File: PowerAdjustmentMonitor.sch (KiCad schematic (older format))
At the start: 19 parts

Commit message: Preliminary Module Layouts
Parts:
- removed R? (x2): R, ~, symbol R
- removed U? (x2): LM324, ~, symbol LM324
- gave numbers to parts that had none: 15
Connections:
- net labels removed: V+_CURR_MON, V-_CURR_MON
- wire segments 96 -> 58

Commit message: Power Modification Module
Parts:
- removed JP2, JP3: JUMPER, ~, symbol JUMPER
- removed R20: RVAR, ~, symbol RVAR
- removed U10: LM317, ~, symbol LM317
- removed U8, U9: 7805, ~, symbol 7805
- added C14, C15, C16, C17, C18, C19, C20, C21, C22, C23, C24, C25: C, ~, symbol C
- added D10, D11, D12, D3, D6, D7, D8, D9: DIODE, ~, symbol DIODE
- added R20, R52, R53, R55: R, ~, symbol R
- added R54: RVAR, ~, symbol RVAR
- added U6: LM317, ~, symbol LM317
- added U7, U8: LM337T, TO-220, symbol LM337T
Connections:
- wire segments 58 -> 108
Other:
- note added: "-1.5 to -10V Output"
- note added: "-10V Output\n"
- note added: "1.5 to 10V Output"
- note added: "10V Output\n"
- moved on the sheet: JP1, R21, R22, R25, R26, R27, R28, U11

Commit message: November 25 Update
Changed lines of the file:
@@
 Sheet 7 9
 Title ""
-Date "27 oct 2013"
+Date "9 nov 2013"
 Rev ""
 Comp ""
@@
 Wire Wire Line
 	5500 5350 5500 4850
-Connection ~ 5300 5350
 Wire Wire Line
 	5500 4450 5500 4000

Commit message: Power Modification Module (check diodes)
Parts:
- D10, D11, D12, D3, D6, D7, D8, D9: value DIODE -> MMBD914-7-F
- R21, R54: value RVAR -> 5K
- R22, R55: value R -> 715
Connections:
- wire segments 108 -> 106

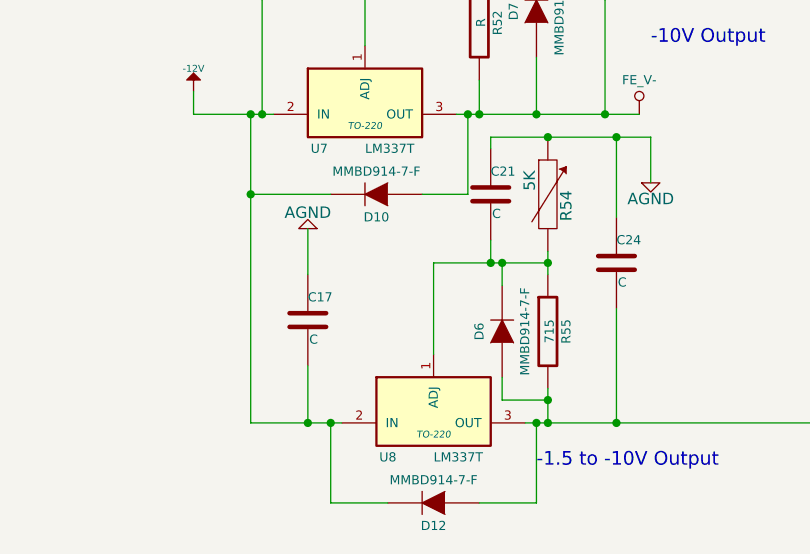
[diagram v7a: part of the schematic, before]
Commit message: Power Modification Module - Correct Diode Polarity
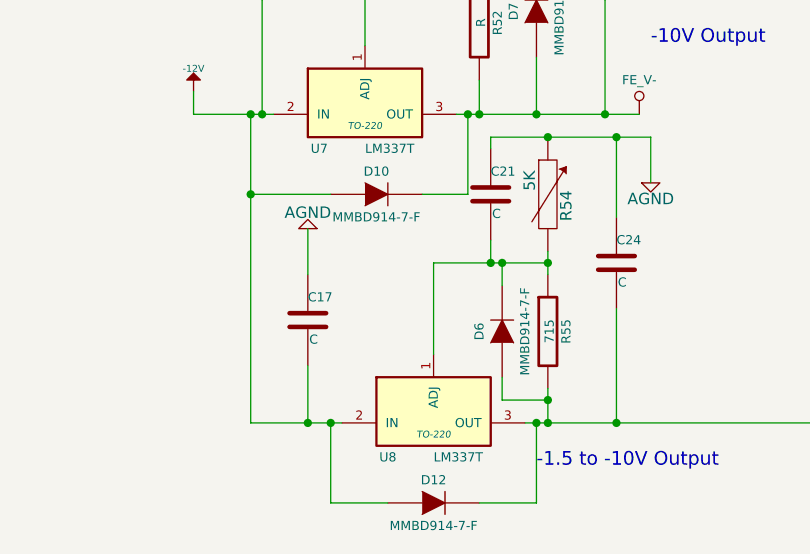
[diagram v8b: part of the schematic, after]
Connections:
- net -12V: now also D10.1 (A), D12.1 (A); no longer D10.2 (K), D12.2 (K)
- net FE_V-: now also D10.2 (K); no longer D10.1 (A)
- net V-_ADJ: now also D12.2 (K); no longer D12.1 (A)
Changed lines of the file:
@@
 Sheet 7 9
 Title ""
-Date "2 dec 2013"
+Date "3 dec 2013"
 Rev ""
 Comp ""
@@
 F 3 "~" H 4500 5700 60  0000 C CNN
 	1    4500 5700
-	-1   0    0    1
+	1    0    0    -1
 $EndComp
 $Comp
@@
 F 3 "~" H 4750 7050 60  0000 C CNN
 	1    4750 7050
-	-1   0    0    1
-$EndComp
-Wire Wire Line
+	1    0    0    -1
+$EndComp
+Wire Wire Line
